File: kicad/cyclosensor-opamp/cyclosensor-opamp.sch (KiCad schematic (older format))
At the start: 12 parts, among them J1 RJ14, U1 LM358

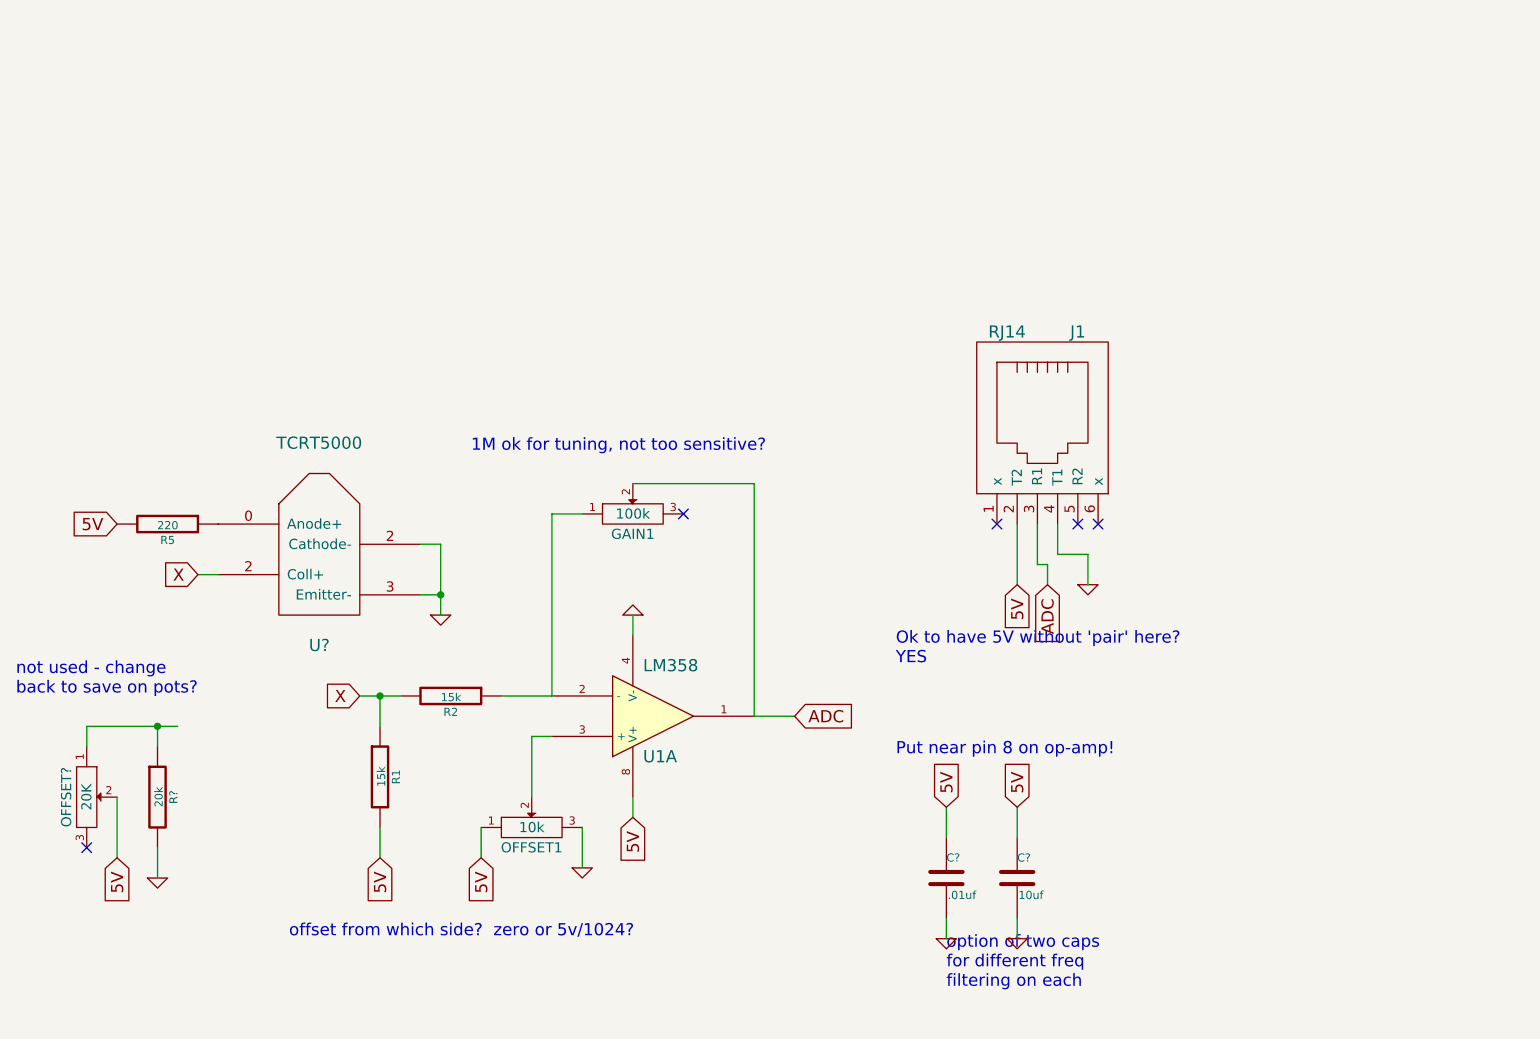
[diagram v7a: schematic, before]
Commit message: change to MCP6001 op amp instead of lm358.  rail to rail, only 5 pins.
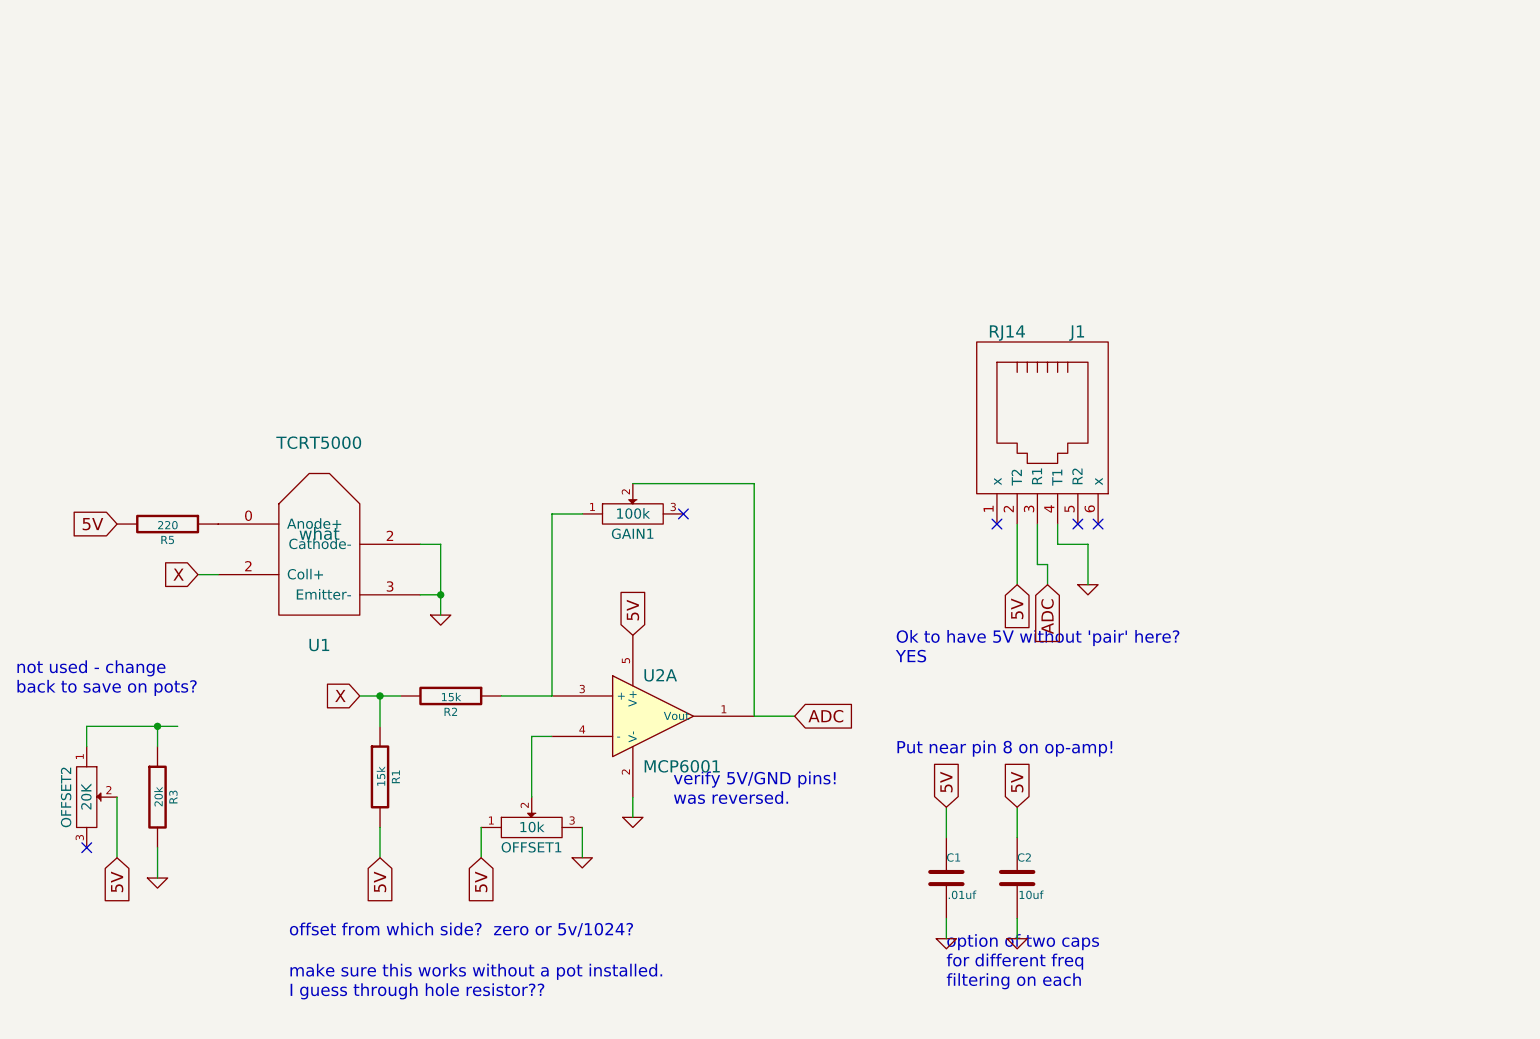
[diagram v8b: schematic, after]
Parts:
- removed U1: LM358, symbol LM358
- added U2: MCP6001, symbol MCP6001
- U1: renamed from U?; footprint ~ -> what
- gave numbers to parts that had none: 4
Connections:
- net 5V: now also U2.5 (V+)
- net ADC: now also U2.1 (Vout)
- net GND: now also U2.2 (V-)
- net at GAIN1.1, R2.1: now also U2.3 (+)
- net at OFFSET1.2: now also U2.4 (-)
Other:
- note added: "make sure this works without a pot installed. \nI guess through hole resistor??"
- note added: "verify 5V/GND pins! \nwas reversed."
- note removed: "1M ok for tuning, not too sensitive?"
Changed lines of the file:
@@
 Sheet 1 1
 Title ""
-Date "16 apr 2014"
+Date "19 apr 2014"
 Rev ""
 Comp ""
@@
 	1    0    0    -1
 $EndComp
-Text GLabel 4900 4950 3    60   Input ~ 0
+Text GLabel 4900 4050 1    60   Input ~ 0
 5V
 $Comp
 L GND #PWR02
 U 1 1 533B8353
-P 4900 3950
-F 0 "#PWR02" H 4900 3950 30  0001 C CNN
-F 1 "GND" H 4900 3880 30  0001 C CNN
-F 2 "" H 4900 3950 60  0000 C CNN
-F 3 "" H 4900 3950 60  0000 C CNN
-	1    4900 3950
-	-1   0    0    1
-$EndComp
-$Comp
-L LM358 U1
-U 1 1 533B83FF
-P 5000 4450
-F 0 "U1" H 4950 4650 60  0000 L CNN
-F 1 "LM358" H 4950 4200 60  0000 L CNN
-F 2 "" H 5000 4450 60  0000 C CNN
-F 3 "" H 5000 4450 60  0000 C CNN
-	1    5000 4450
-	1    0    0    1
+P 4900 4950
+F 0 "#PWR02" H 4900 4950 30  0001 C CNN
+F 1 "GND" H 4900 4880 30  0001 C CNN
+F 2 "" H 4900 4950 60  0000 C CNN
+F 3 "" H 4900 4950 60  0000 C CNN
+	1    4900 4950
+	1    0    0    -1
 $EndComp
 $Comp
@@
 5V
 $Comp
-L GND #PWR05
+L GND #PWR03
 U 1 1 533B9F2F
 P 3950 3950
-F 0 "#PWR05" H 3950 3950 30  0001 C CNN
+F 0 "#PWR03" H 3950 3950 30  0001 C CNN
 F 1 "GND" H 3950 3880 30  0001 C CNN
 F 2 "" H 3950 3950 60  0000 C CNN
@@
 Text Notes 3200 5550 0    60   ~ 0
 offset from which side?  zero or 5v/1024?
-Text Notes 4100 3150 0    60   ~ 0
-1M ok for tuning, not too sensitive?
-$Comp
-L C C?
+$Comp
+L C C1
 U 1 1 53449FBF
 P 6450 5250
-F 0 "C?" H 6450 5350 40  0000 L CNN
+F 0 "C1" H 6450 5350 40  0000 L CNN
 F 1 ".01uf" H 6456 5165 40  0000 L CNN
 F 2 "~" H 6488 5100 30  0000 C CNN
@@
 5V
 $Comp
-L GND #PWR?
+L GND #PWR04
 U 1 1 53449FDD
 P 6450 5550
-F 0 "#PWR?" H 6450 5550 30  0001 C CNN
+F 0 "#PWR04" H 6450 5550 30  0001 C CNN
 F 1 "GND" H 6450 5480 30  0001 C CNN
 F 2 "" H 6450 5550 60  0000 C CNN
@@
 Put near pin 8 on op-amp!
 $Comp
-L C C?
+L C C2
 U 1 1 5344A0AE
 P 6800 5250
-F 0 "C?" H 6800 5350 40  0000 L CNN
+F 0 "C2" H 6800 5350 40  0000 L CNN
 F 1 "10uf" H 6806 5165 40  0000 L CNN
 F 2 "~" H 6838 5100 30  0000 C CNN
@@
 5V
 $Comp
-L GND #PWR?
+L GND #PWR05
 U 1 1 5344A0B5
 P 6800 5550
-F 0 "#PWR?" H 6800 5550 30  0001 C CNN
+F 0 "#PWR05" H 6800 5550 30  0001 C CNN
 F 1 "GND" H 6800 5480 30  0001 C CNN
 F 2 "" H 6800 5550 60  0000 C CNN
@@
 option of two caps \nfor different freq\nfiltering on each
 $Comp
-L TCRT5000 U?
+L TCRT5000 U1
 U 1 1 53499E1E
 P 3350 3550
-F 0 "U?" H 3350 3000 60  0000 C CNN
+F 0 "U1" H 3350 3000 60  0000 C CNN
 F 1 "TCRT5000" H 3350 4000 60  0000 C CNN
-F 2 "~" H 3350 3550 60  0000 C CNN
+F 2 "what" H 3350 3550 60  0000 C CNN
 F 3 "~" H 3350 3550 60  0000 C CNN
 	1    3350 3550
@@
 $EndComp
 Wire Wire Line
-	7000 3500 7000 3650
-Wire Wire Line
-	7000 3650 7150 3650
-Wire Wire Line
 	4500 3450 4500 4350
 Wire Wire Line
@@
 	3650 5000 3650 5150
 Wire Wire Line
-	4900 3950 4900 4050
-Wire Wire Line
 	6900 3500 6900 3700
 Wire Wire Line
@@
 Wire Wire Line
 	4500 3450 4650 3450
-Wire Wire Line
-	4900 4850 4900 4950
-Wire Wire Line
-	7150 3650 7150 3800
 Wire Wire Line
 	6800 3800 6800 3500
@@
 5V
 $Comp
-L R R?
+L R R3
 U 1 1 5349C83F
 P 2550 4850
-F 0 "R?" V 2630 4850 40  0000 C CNN
+F 0 "R3" V 2630 4850 40  0000 C CNN
 F 1 "20k" V 2557 4851 40  0000 C CNN
 F 2 "~" V 2480 4850 30  0000 C CNN
@@
 $EndComp
 $Comp
-L GND #PWR?
+L GND #PWR06
 U 1 1 5349C845
 P 2550 5250
-F 0 "#PWR?" H 2550 5250 30  0001 C CNN
+F 0 "#PWR06" H 2550 5250 30  0001 C CNN
 F 1 "GND" H 2550 5180 30  0001 C CNN
 F 2 "" H 2550 5250 60  0000 C CNN
@@
 $EndComp
 $Comp
-L POT OFFSET?
+L POT OFFSET2
 U 1 1 5349C84B
 P 2200 4850
-F 0 "OFFSET?" H 2200 4750 50  0000 C CNN
+F 0 "OFFSET2" H 2200 4750 50  0000 C CNN
 F 1 "20K" H 2200 4850 50  0000 C CNN
 F 2 "~" H 2200 4850 60  0000 C CNN
@@
 	2350 4850 2350 5150
 $Comp
-L GND #PWR?
+L GND #PWR07
 U 1 1 5349C88D
-P 4650 5200
-F 0 "#PWR?" H 4650 5200 30  0001 C CNN
-F 1 "GND" H 4650 5130 30  0001 C CNN
-F 2 "" H 4650 5200 60  0000 C CNN
-F 3 "" H 4650 5200 60  0000 C CNN
-	1    4650 5200
+P 4650 5150
+F 0 "#PWR07" H 4650 5150 30  0001 C CNN
+F 1 "GND" H 4650 5080 30  0001 C CNN
+F 2 "" H 4650 5150 60  0000 C CNN
+F 3 "" H 4650 5150 60  0000 C CNN
+	1    4650 5150
 	1    0    0    -1
 $EndComp
@@
 Text Notes 1850 4350 0    60   ~ 0
 not used - change\nback to save on pots?
-Wire Wire Line
-	4650 5000 4650 5200
+$Comp
+L MCP6001 U2
+U 1 1 53518B31
+P 5000 4450
+F 0 "U2" H 4950 4650 60  0000 L CNN
+F 1 "MCP6001" H 4950 4200 60  0000 L CNN
+F 2 "" H 5000 4450 60  0000 C CNN
+F 3 "" H 5000 4450 60  0000 C CNN
+	1    5000 4450
+	1    0    0    -1
+$EndComp
+Wire Wire Line
+	4900 4850 4900 4950
+Wire Wire Line
+	4650 5150 4650 5000
+Wire Wire Line
+	7000 3500 7000 3600
+Wire Wire Line
+	7000 3600 7150 3600
+Wire Wire Line
+	7150 3600 7150 3800
+Text Notes 5100 4900 0    60   ~ 0
+verify 5V/GND pins!  \nwas reversed.
+Text Notes 3200 5850 0    60   ~ 0
+make sure this works without a pot installed.  \nI guess through hole resistor??
 $EndSCHEMATC
